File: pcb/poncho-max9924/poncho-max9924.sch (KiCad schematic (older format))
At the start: 50 parts

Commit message: avances en el esquematico
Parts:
- removed JP? (x3): Jumper_2_Open, symbol Jumper:Jumper_2_Open
- removed R? (x2): R_US, symbol Device:R_US
- added J?: Screw_Terminal_01x02, symbol Connector:Screw_Terminal_01x02
- added JP?: jumper_4_open, symbol custom_jumpers:jumper_4_open
- C?: value C -> 4.7uF
- C? (x4): value C -> 0.1uF
- C?: value C -> 1000pF
- C?: value C -> 1uF
- C?: value C -> 220pF
- R? (x6): value R_US -> OPEN
- R? (x4): value R_US -> 4.99K 1%
- R? (x2): value R_US -> 1K 1%
- R?: value R_US -> 39.2K 1%
- R?: value R_US -> 68.1K 1%
- R?: value R_US -> 10K 1%
- R?: value R_US -> 10K
- R?: value R_US -> 100K 1%
- R?: value R_US -> 54.9K 1%
- R?: value R_US -> 464K 1%
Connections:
- wire segments 164 -> 161
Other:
- note added: "Contador de pulsos"
- note added: "Generador de onda triangular"
- moved on the sheet: C?, JP?, R?, TP?, U?

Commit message: Esquematico listo para primer revision
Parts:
- added J2: Screw_Terminal_01x02, symbol Connector:Screw_Terminal_01x02
- added TP1: TestPoint, symbol Connector:TestPoint
- U1, U2: renamed from U?; Manufacturer (none) -> MAXIM
- gave numbers to parts that had none: 44
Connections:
- net labels added: +5V
- net labels removed: VCC
- wire segments 161 -> 211
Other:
- note added: "Conectores EDU-CIAA"
- moved on the sheet: C1, C10, C2, C3, C4, C5, C6, C7, C8, C9, J1, JP1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

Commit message: Se realizaron correcciones en base a comentarios del revisor M. Castello
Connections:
- net labels removed: DIV_BIAS, SENSE+, SENSE-
- no-connect marks 0 -> 56
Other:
- moved on the sheet: J1
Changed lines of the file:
@@
 	1    0    0    -1
 $EndComp
-Text GLabel 6500 1950 2    50   Input ~ 0
-FILTER
 $Comp
 L Device:R_US R1
@@
 	1    0    0    -1
 $EndComp
-Text GLabel 3100 2650 0    50   Input ~ 0
-BIAS
 $Comp
 L power:GND #PWR07
 U 1 1 60F4090E
-P 3600 3300
-F 0 "#PWR07" H 3600 3050 50  0001 C CNN
-F 1 "GND" H 3605 3127 50  0001 C CNN
-F 2 "" H 3600 3300 50  0001 C CNN
-F 3 "" H 3600 3300 50  0001 C CNN
-	1    3600 3300
+P 3600 3400
+F 0 "#PWR07" H 3600 3150 50  0001 C CNN
+F 1 "GND" H 3605 3227 50  0001 C CNN
+F 2 "" H 3600 3400 50  0001 C CNN
+F 3 "" H 3600 3400 50  0001 C CNN
+	1    3600 3400
 	1    0    0    -1
 $EndComp
@@
 $EndComp
 Connection ~ 2450 1350
-Text GLabel 2950 1050 0    50   Input ~ 0
-AOUT
-Text GLabel 4300 1350 2    50   Input ~ 0
-BIAS
-Wire Wire Line
-	4200 1350 4300 1350
 $Comp
 L Device:Jumper_NO_Small JP3
@@
 Wire Wire Line
 	9900 2600 10000 2600
-Text GLabel 10000 2050 2    50   Input ~ 0
-COUT_2
-Wire Wire Line
-	9900 2050 10000 2050
 Connection ~ 9900 2050
 $Comp
@@
 	1    0    0    -1
 $EndComp
-Text GLabel 10700 1150 2    50   Input ~ 0
-AOUT
 $Comp
 L Device:Jumper_NO_Small JP7
@@
 	0    1    1    0
 $EndComp
-Text GLabel 8300 1050 2    50   Input ~ 0
-COUT_2
 Wire Wire Line
 	7950 1350 8250 1350
 Wire Wire Line
 	8250 1350 8250 1050
-Wire Wire Line
-	8250 1050 8300 1050
 Wire Wire Line
 	8200 1050 8250 1050
@@
 	0    1    1    0
 $EndComp
-Text GLabel 6850 3250 2    50   Input ~ 0
-COUT
 $Comp
 L custom_jumpers:jumper_4_open JP5
@@
 Connection ~ 3600 3150
 Wire Wire Line
-	3600 3150 3600 3300
-Wire Wire Line
 	3400 2950 3450 2950
 Wire Wire Line
@@
 L power:GND #PWR04
 U 1 1 611E2147
-P 2850 3350
-F 0 "#PWR04" H 2850 3100 50  0001 C CNN
-F 1 "GND" H 2855 3177 50  0001 C CNN
-F 2 "" H 2850 3350 50  0001 C CNN
-F 3 "" H 2850 3350 50  0001 C CNN
-	1    2850 3350
-	1    0    0    -1
-$EndComp
-Wire Wire Line
-	2850 3300 2850 3350
+P 2850 3400
+F 0 "#PWR04" H 2850 3150 50  0001 C CNN
+F 1 "GND" H 2855 3227 50  0001 C CNN
+F 2 "" H 2850 3400 50  0001 C CNN
+F 3 "" H 2850 3400 50  0001 C CNN
+	1    2850 3400
+	1    0    0    -1
+$EndComp
 $Comp
 L power:GND #PWR03
@@
 Wire Wire Line
 	3150 2650 3600 2650
-Wire Wire Line
-	3100 2650 3150 2650
 Connection ~ 3150 2650
 Wire Wire Line
@@
 	3000 1350 3850 1350
 Wire Wire Line
-	2950 1050 3000 1050
-Wire Wire Line
-	3000 1050 3000 1350
-Wire Wire Line
 	2750 2250 3000 2250
 Connection ~ 2750 2250
@@
 Wire Wire Line
 	9550 1500 9350 1500
-Wire Wire Line
-	10650 1150 10700 1150
 Wire Wire Line
 	10400 1150 10400 2600
@@
 	1950 2250 2050 2250
 Wire Wire Line
-	1350 3350 1350 3400
-Wire Wire Line
 	1350 2850 1350 2950
 Wire Wire Line
@@
 L Connector:Screw_Terminal_01x02 J1
 U 1 1 61577878
-P 1050 1450
-F 0 "J1" H 1050 1200 50  0000 C CNN
-F 1 "Screw_Terminal_01x02" H 968 1216 50  0001 C CNN
-F 2 "" H 1050 1450 50  0001 C CNN
-F 3 "~" H 1050 1450 50  0001 C CNN
-	1    1050 1450
+P 1200 1450
+F 0 "J1" H 1200 1200 50  0000 C CNN
+F 1 "Screw_Terminal_01x02" H 1118 1216 50  0001 C CNN
+F 2 "" H 1200 1450 50  0001 C CNN
+F 3 "~" H 1200 1450 50  0001 C CNN
+	1    1200 1450
 	-1   0    0    1
 $EndComp
@@
 	1    0    0    -1
 $EndComp
-Text GLabel 5550 5850 2    50   Input ~ 0
-COUT
-Wire Wire Line
-	5450 5850 5550 5850
 Wire Wire Line
 	2450 1750 2450 1800
@@
 	5550 2250 5550 2050
 Wire Wire Line
-	4900 2450 5400 2450
-Wire Wire Line
 	5550 1650 5650 1650
 Wire Wire Line
@@
 	6350 2050 6350 1950
 Wire Wire Line
-	6350 1950 6500 1950
-Wire Wire Line
 	5550 2650 5550 2750
 Wire Wire Line
@@
 Wire Wire Line
 	5850 2750 5950 2750
-Text GLabel 6300 2750 2    50   Input ~ 0
-BIAS
-Wire Wire Line
-	6250 2750 6300 2750
 $Comp
 L Connector:Screw_Terminal_01x02 J2
@@
 Wire Wire Line
 	6850 2750 6900 2750
-Text GLabel 5550 5950 2    50   Input ~ 0
-FILTER
-Wire Wire Line
-	5450 5950 5550 5950
-Text Label 6600 2650 0    50   ~ 0
-V_PULL
 Wire Wire Line
 	5550 3050 5650 3050
@@
 Wire Wire Line
 	6000 3050 6050 3050
-Connection ~ 6000 3250
-Wire Wire Line
-	6000 3250 6850 3250
 Wire Wire Line
 	6350 3050 6600 3050
@@
 Wire Wire Line
 	6600 2650 6900 2650
-Text Label 2050 1800 0    50   ~ 0
-DIV_BIAS
 Wire Wire Line
 	1900 1750 1900 1800
 Wire Wire Line
 	1900 1800 2450 1800
-Text Label 1350 1350 0    50   ~ 0
-SENSE+
-Text Label 1350 2250 0    50   ~ 0
-SENSE-
 Wire Wire Line
 	3000 5250 3050 5250
@@
 Wire Wire Line
 	4250 6250 4200 6250
-Connection ~ 4200 6250
 Wire Wire Line
 	3000 4450 3050 4450
@@
 Wire Wire Line
 	3050 6250 3050 6500
-Wire Wire Line
-	4200 6250 4200 6500
 Wire Notes Line
 	1700 6750 5900 6750
@@
 Conectores EDU-CIAA
 Wire Wire Line
-	1250 1350 1650 1350
-Wire Wire Line
-	1250 1450 1300 1450
-Wire Wire Line
-	1300 1450 1300 2250
-Wire Wire Line
-	1300 2250 1650 2250
+	5450 5850 5800 5850
+Text Label 5550 5850 0    50   ~ 0
+COUT
+Wire Wire Line
+	5450 5950 5800 5950
+Text Label 5550 5950 0    50   ~ 0
+FILTER
+Wire Wire Line
+	6350 1950 6850 1950
+Text Label 6600 1950 0    50   ~ 0
+FILTER
+Text Label 6600 2650 0    50   ~ 0
+V_PULL
+Text Label 6300 2750 0    50   ~ 0
+BIAS
+Wire Wire Line
+	6250 2750 6450 2750
+Text Label 6300 3250 0    50   ~ 0
+COUT
+Wire Wire Line
+	6000 3250 6500 3250
+Connection ~ 6000 3250
+Wire Wire Line
+	9900 2050 10250 2050
+Text Label 9950 2050 0    50   ~ 0
+COUT_2
+Wire Wire Line
+	8250 1050 8650 1050
+Text Label 8350 1050 0    50   ~ 0
+COUT_2
+Wire Wire Line
+	10650 1150 10950 1150
+Text Label 10750 1150 0    50   ~ 0
+AOUT
+Wire Wire Line
+	3000 1350 3000 1200
+Wire Wire Line
+	3000 1200 3300 1200
+Text Label 3100 1200 0    50   ~ 0
+AOUT
+Wire Wire Line
+	4200 1350 4550 1350
+Text Label 4350 1350 0    50   ~ 0
+BIAS
+Wire Wire Line
+	2900 2650 3150 2650
+Text Label 2900 2650 0    50   ~ 0
+BIAS
+NoConn ~ 1800 4350
+NoConn ~ 1800 4450
+NoConn ~ 1800 4550
+NoConn ~ 1800 4650
+NoConn ~ 1800 4750
+NoConn ~ 1800 4850
+NoConn ~ 1800 4950
+NoConn ~ 1800 5050
+NoConn ~ 1800 5150
+NoConn ~ 1800 5250
+NoConn ~ 1800 5350
+NoConn ~ 1800 5450
+NoConn ~ 1800 5550
+NoConn ~ 1800 5650
+NoConn ~ 1800 5750
+NoConn ~ 1800 5850
+NoConn ~ 1800 5950
+NoConn ~ 1800 6050
+NoConn ~ 1800 6150
+NoConn ~ 1800 6250
+NoConn ~ 3000 6050
+NoConn ~ 3000 5950
+NoConn ~ 3000 5150
+NoConn ~ 3000 5050
+NoConn ~ 3000 4950
+NoConn ~ 3000 4850
+NoConn ~ 3000 4750
+NoConn ~ 3000 4650
+NoConn ~ 3000 4550
+NoConn ~ 4250 4750
+NoConn ~ 4250 4350
+NoConn ~ 4250 5050
+NoConn ~ 4250 5350
+NoConn ~ 4250 5450
+NoConn ~ 4250 5750
+NoConn ~ 4250 5850
+NoConn ~ 4250 5950
+NoConn ~ 4250 6050
+NoConn ~ 5450 6250
+NoConn ~ 5450 6150
+NoConn ~ 5450 6050
+NoConn ~ 5450 5750
+NoConn ~ 5450 5650
+NoConn ~ 5450 5550
+NoConn ~ 5450 5450
+NoConn ~ 5450 5350
+NoConn ~ 5450 5250
+NoConn ~ 5450 5150
+NoConn ~ 5450 5050
+NoConn ~ 5450 4950
+NoConn ~ 5450 4850
+NoConn ~ 5450 4750
+NoConn ~ 5450 4650
+NoConn ~ 5450 4550
+NoConn ~ 5450 4450
+NoConn ~ 5450 4350
+Wire Wire Line
+	1350 3350 1350 3400
+Wire Wire Line
+	5400 2450 4900 2450
+Wire Wire Line
+	2850 3300 2850 3400
+Wire Wire Line
+	3600 3150 3600 3400
+Wire Wire Line
+	1650 1350 1400 1350
+Wire Wire Line
+	1400 1450 1500 1450
+Wire Wire Line
+	1500 1450 1500 2250
+Wire Wire Line
+	1500 2250 1650 2250
+Wire Wire Line
+	4200 6250 4200 6500
+Connection ~ 4200 6250
 $EndSCHEMATC

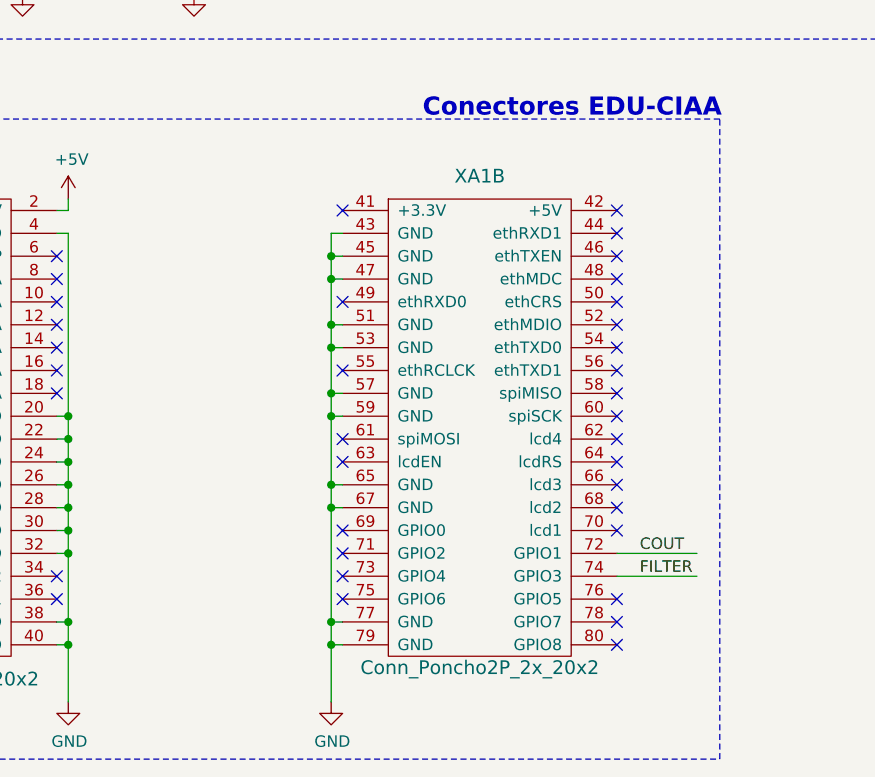
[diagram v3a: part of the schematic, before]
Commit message: Correccion de error ERC en terminal de masa
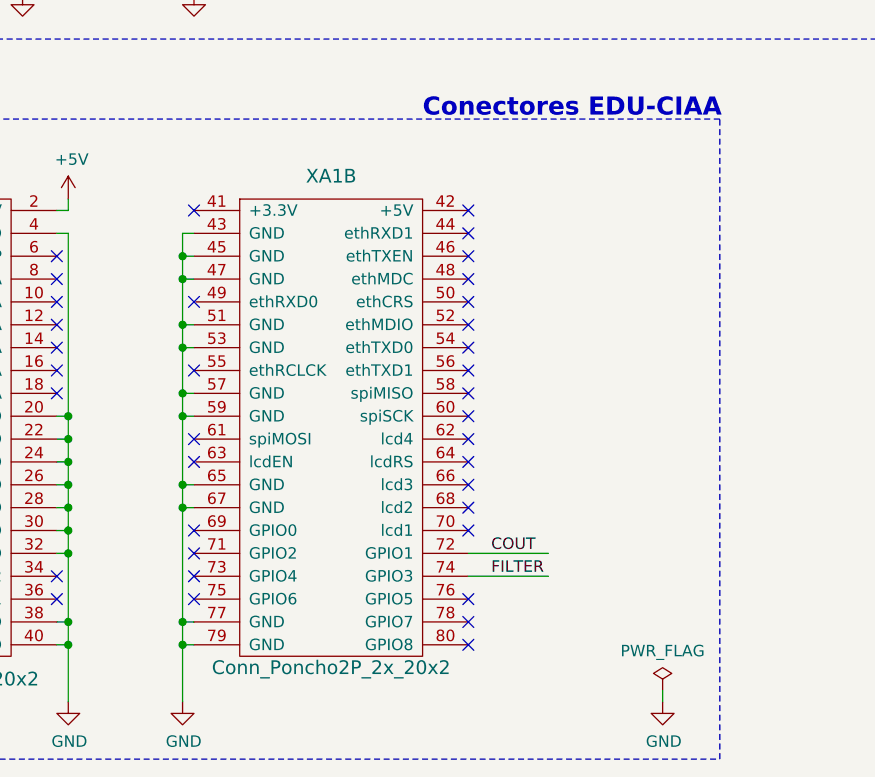
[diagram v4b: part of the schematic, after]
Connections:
- wire segments 211 -> 212
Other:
- moved on the sheet: XA1B
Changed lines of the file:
@@
 L Poncho_Esqueleto:Conn_Poncho2P_2x_20x2 XA1
 U 2 1 60EA5F6F
-P 4500 4650
-F 0 "XA1" H 4850 5100 60  0000 C CNN
-F 1 "Conn_Poncho2P_2x_20x2" H 4850 2950 60  0000 C CNN
-F 2 "" H 4500 4650 60  0000 C CNN
-F 3 "" H 4500 4650 60  0000 C CNN
-	2    4500 4650
+P 3850 4650
+F 0 "XA1" H 4200 5100 60  0000 C CNN
+F 1 "Conn_Poncho2P_2x_20x2" H 4200 2950 60  0000 C CNN
+F 2 "" H 3850 4650 60  0000 C CNN
+F 3 "" H 3850 4650 60  0000 C CNN
+	2    3850 4650
 	1    0    0    -1
 $EndComp
@@
 L power:GND #PWR08
 U 1 1 60FC6A2E
-P 4200 6500
-F 0 "#PWR08" H 4200 6250 50  0001 C CNN
-F 1 "GND" H 4205 6327 50  0000 C CNN
-F 2 "" H 4200 6500 50  0001 C CNN
-F 3 "" H 4200 6500 50  0001 C CNN
-	1    4200 6500
+P 3550 6500
+F 0 "#PWR08" H 3550 6250 50  0001 C CNN
+F 1 "GND" H 3555 6327 50  0000 C CNN
+F 2 "" H 3550 6500 50  0001 C CNN
+F 3 "" H 3550 6500 50  0001 C CNN
+	1    3550 6500
 	1    0    0    -1
 $EndComp
@@
 	3050 5850 3050 6150
 Wire Wire Line
-	4200 4450 4200 4550
-Wire Wire Line
-	4250 4450 4200 4450
-Wire Wire Line
-	4250 4550 4200 4550
-Connection ~ 4200 4550
-Wire Wire Line
-	4200 4550 4200 4650
-Wire Wire Line
-	4250 4650 4200 4650
-Connection ~ 4200 4650
-Wire Wire Line
-	4200 4650 4200 4850
-Wire Wire Line
-	4250 4850 4200 4850
-Connection ~ 4200 4850
-Wire Wire Line
-	4200 4850 4200 4950
-Wire Wire Line
-	4250 4950 4200 4950
-Connection ~ 4200 4950
-Wire Wire Line
-	4200 4950 4200 5150
-Wire Wire Line
-	4250 5150 4200 5150
-Connection ~ 4200 5150
-Wire Wire Line
-	4200 5150 4200 5250
-Wire Wire Line
-	4250 5250 4200 5250
-Connection ~ 4200 5250
-Wire Wire Line
-	4200 5250 4200 5550
-Wire Wire Line
-	4250 5550 4200 5550
-Connection ~ 4200 5550
-Wire Wire Line
-	4200 5550 4200 5650
-Wire Wire Line
-	4250 5650 4200 5650
-Connection ~ 4200 5650
-Wire Wire Line
-	4200 5650 4200 6150
-Wire Wire Line
-	4250 6150 4200 6150
-Connection ~ 4200 6150
-Wire Wire Line
-	4200 6150 4200 6250
-Wire Wire Line
-	4250 6250 4200 6250
+	3550 4450 3550 4550
+Wire Wire Line
+	3600 4450 3550 4450
+Wire Wire Line
+	3600 4550 3550 4550
+Connection ~ 3550 4550
+Wire Wire Line
+	3550 4550 3550 4650
+Wire Wire Line
+	3600 4650 3550 4650
+Connection ~ 3550 4650
+Wire Wire Line
+	3550 4650 3550 4850
+Wire Wire Line
+	3600 4850 3550 4850
+Connection ~ 3550 4850
+Wire Wire Line
+	3550 4850 3550 4950
+Wire Wire Line
+	3600 4950 3550 4950
+Connection ~ 3550 4950
+Wire Wire Line
+	3550 4950 3550 5150
+Wire Wire Line
+	3600 5150 3550 5150
+Connection ~ 3550 5150
+Wire Wire Line
+	3550 5150 3550 5250
+Wire Wire Line
+	3600 5250 3550 5250
+Connection ~ 3550 5250
+Wire Wire Line
+	3550 5250 3550 5550
+Wire Wire Line
+	3600 5550 3550 5550
+Connection ~ 3550 5550
+Wire Wire Line
+	3550 5550 3550 5650
+Wire Wire Line
+	3600 5650 3550 5650
+Connection ~ 3550 5650
+Wire Wire Line
+	3550 5650 3550 6150
+Wire Wire Line
+	3600 6150 3550 6150
+Connection ~ 3550 6150
+Wire Wire Line
+	3550 6150 3550 6250
+Wire Wire Line
+	3600 6250 3550 6250
 Wire Wire Line
 	3000 4450 3050 4450
@@
 Conectores EDU-CIAA
 Wire Wire Line
-	5450 5850 5800 5850
-Text Label 5550 5850 0    50   ~ 0
+	4800 5850 5150 5850
+Text Label 4900 5850 0    50   ~ 0
 COUT
 Wire Wire Line
-	5450 5950 5800 5950
-Text Label 5550 5950 0    50   ~ 0
+	4800 5950 5150 5950
+Text Label 4900 5950 0    50   ~ 0
 FILTER
 Wire Wire Line
@@
 NoConn ~ 3000 4650
 NoConn ~ 3000 4550
-NoConn ~ 4250 4750
-NoConn ~ 4250 4350
-NoConn ~ 4250 5050
-NoConn ~ 4250 5350
-NoConn ~ 4250 5450
-NoConn ~ 4250 5750
-NoConn ~ 4250 5850
-NoConn ~ 4250 5950
-NoConn ~ 4250 6050
-NoConn ~ 5450 6250
-NoConn ~ 5450 6150
-NoConn ~ 5450 6050
-NoConn ~ 5450 5750
-NoConn ~ 5450 5650
-NoConn ~ 5450 5550
-NoConn ~ 5450 5450
-NoConn ~ 5450 5350
-NoConn ~ 5450 5250
-NoConn ~ 5450 5150
-NoConn ~ 5450 5050
-NoConn ~ 5450 4950
-NoConn ~ 5450 4850
-NoConn ~ 5450 4750
-NoConn ~ 5450 4650
-NoConn ~ 5450 4550
-NoConn ~ 5450 4450
-NoConn ~ 5450 4350
+NoConn ~ 3600 4750
+NoConn ~ 3600 4350
+NoConn ~ 3600 5050
+NoConn ~ 3600 5350
+NoConn ~ 3600 5450
+NoConn ~ 3600 5750
+NoConn ~ 3600 5850
+NoConn ~ 3600 5950
+NoConn ~ 3600 6050
+NoConn ~ 4800 6250
+NoConn ~ 4800 6150
+NoConn ~ 4800 6050
+NoConn ~ 4800 5750
+NoConn ~ 4800 5650
+NoConn ~ 4800 5550
+NoConn ~ 4800 5450
+NoConn ~ 4800 5350
+NoConn ~ 4800 5250
+NoConn ~ 4800 5150
+NoConn ~ 4800 5050
+NoConn ~ 4800 4950
+NoConn ~ 4800 4850
+NoConn ~ 4800 4750
+NoConn ~ 4800 4650
+NoConn ~ 4800 4550
+NoConn ~ 4800 4450
+NoConn ~ 4800 4350
 Wire Wire Line
 	1350 3350 1350 3400
@@
 	1500 2250 1650 2250
 Wire Wire Line
-	4200 6250 4200 6500
-Connection ~ 4200 6250
+	3550 6250 3550 6500
+Connection ~ 3550 6250
+$Comp
+L power:PWR_FLAG #FLG?
+U 1 1 60FA87B0
+P 5650 6450
+F 0 "#FLG?" H 5650 6525 50  0001 C CNN
+F 1 "PWR_FLAG" H 5650 6623 50  0000 C CNN
+F 2 "" H 5650 6450 50  0001 C CNN
+F 3 "~" H 5650 6450 50  0001 C CNN
+	1    5650 6450
+	1    0    0    -1
+$EndComp
+$Comp
+L power:GND #PWR?
+U 1 1 60FA8C97
+P 5650 6500
+F 0 "#PWR?" H 5650 6250 50  0001 C CNN
+F 1 "GND" H 5655 6327 50  0000 C CNN
+F 2 "" H 5650 6500 50  0001 C CNN
+F 3 "" H 5650 6500 50  0001 C CNN
+	1    5650 6500
+	1    0    0    -1
+$EndComp
+Wire Wire Line
+	5650 6450 5650 6500
 $EndSCHEMATC

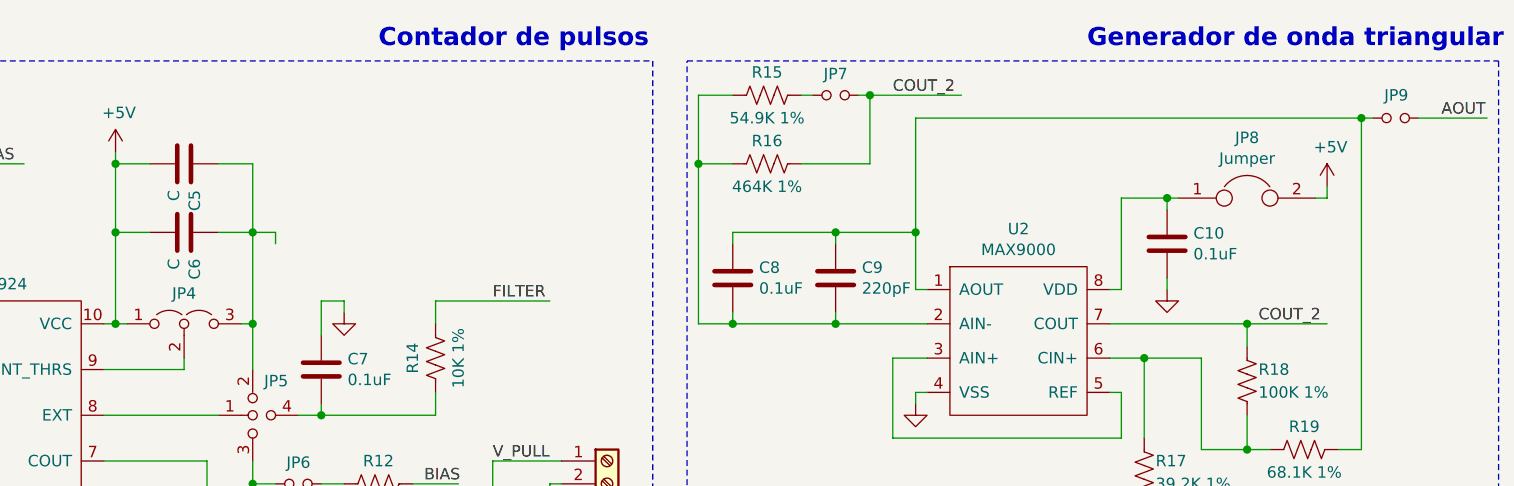
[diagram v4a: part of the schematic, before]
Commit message: Se crearon huellas faltantes. Se asignaron huellas a todos los componentes y se hizo una primera ubicacion de componentes en el circuito impreso
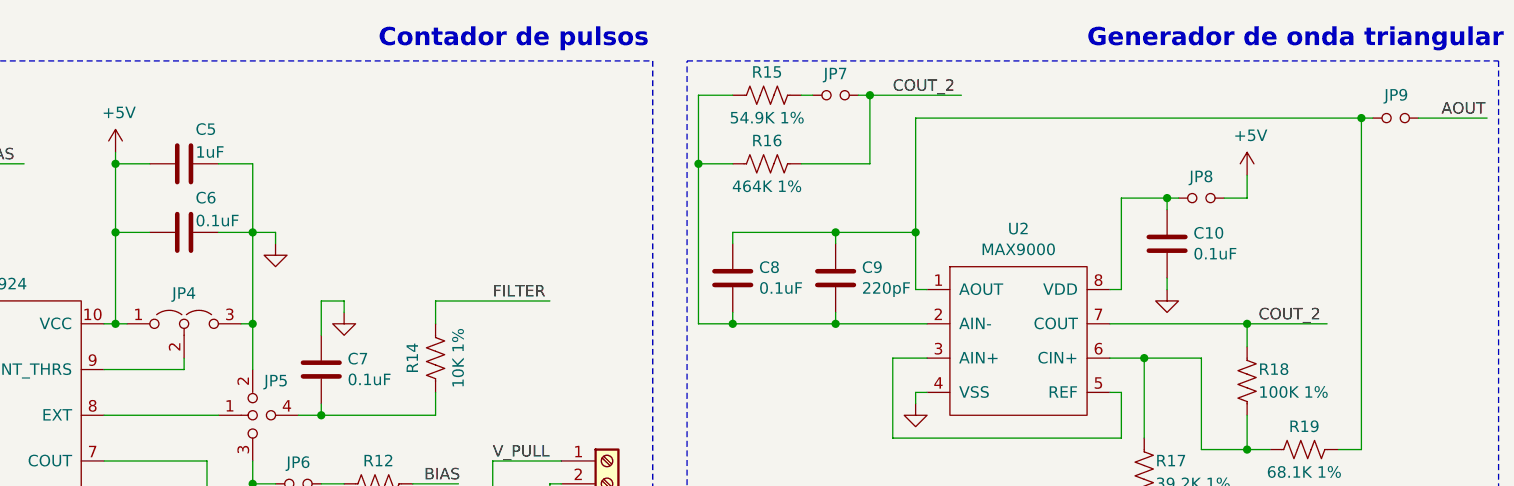
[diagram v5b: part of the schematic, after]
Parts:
- removed JP8: Jumper, symbol Device:Jumper
- added JP8: Jumper_NO_Small, Connector_PinHeader_2.54mm:PinHeader_1x02_P2.54mm_Vertical, symbol Device:Jumper_NO_Small
- C1, C10, C2, C3, C4, C7, C8, C9: footprint (none) -> Capacitor_SMD:C_0805_2012Metric_Pad1.18x1.45mm_HandSolder
- C5: value C -> 1uF; footprint (none) -> Capacitor_SMD:C_0805_2012Metric_Pad1.18x1.45mm_HandSolder
- C6: value C -> 0.1uF; footprint (none) -> Capacitor_SMD:C_0805_2012Metric_Pad1.18x1.45mm_HandSolder
- J1, J2: footprint (none) -> TerminalBlock:TerminalBlock_bornier-2_P5.08mm
- JP1, JP3, JP6, JP7, JP9: footprint (none) -> Connector_PinHeader_2.54mm:PinHeader_1x02_P2.54mm_Vertical
- JP2, JP4: footprint (none) -> Connector_PinHeader_2.54mm:PinHeader_1x03_P2.54mm_Vertical
- JP5: footprint (none) -> misc:PinHeader_1x03_1x01_P2.54mm_Vertical
- R1, R10, R11, R12, R13, R14, R15, R16, R17, R18, R19, R2, R3, R4, R5, R6, R7, R8, R9: footprint (none) -> Resistor_SMD:R_0805_2012Metric_Pad1.20x1.40mm_HandSolder
- TP1, TP2, TP3, TP4, TP5: footprint (none) -> TestPoint:TestPoint_Pad_D2.0mm
- U1: footprint (none) -> umax:UMAX10
- U2: footprint (none) -> umax:UMAX8
- XA1: footprint (none) -> Poncho_Esqueleto:Conn_Poncho_Mediano
